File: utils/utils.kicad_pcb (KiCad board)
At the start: 2 copper layers, 26 parts, among them J1 1_AIN, J10 2_OUT, J11 EURORACK_CONN_16, J2 1_BIN, J3 1_GATE, J4 2_AIN, J5 2_BIN, J6 2_GATE, J7 1_~OUT, J8 2_~OUT, J9 1_OUT, Q1 2N7000, Q2 2N7000, U1 TL074

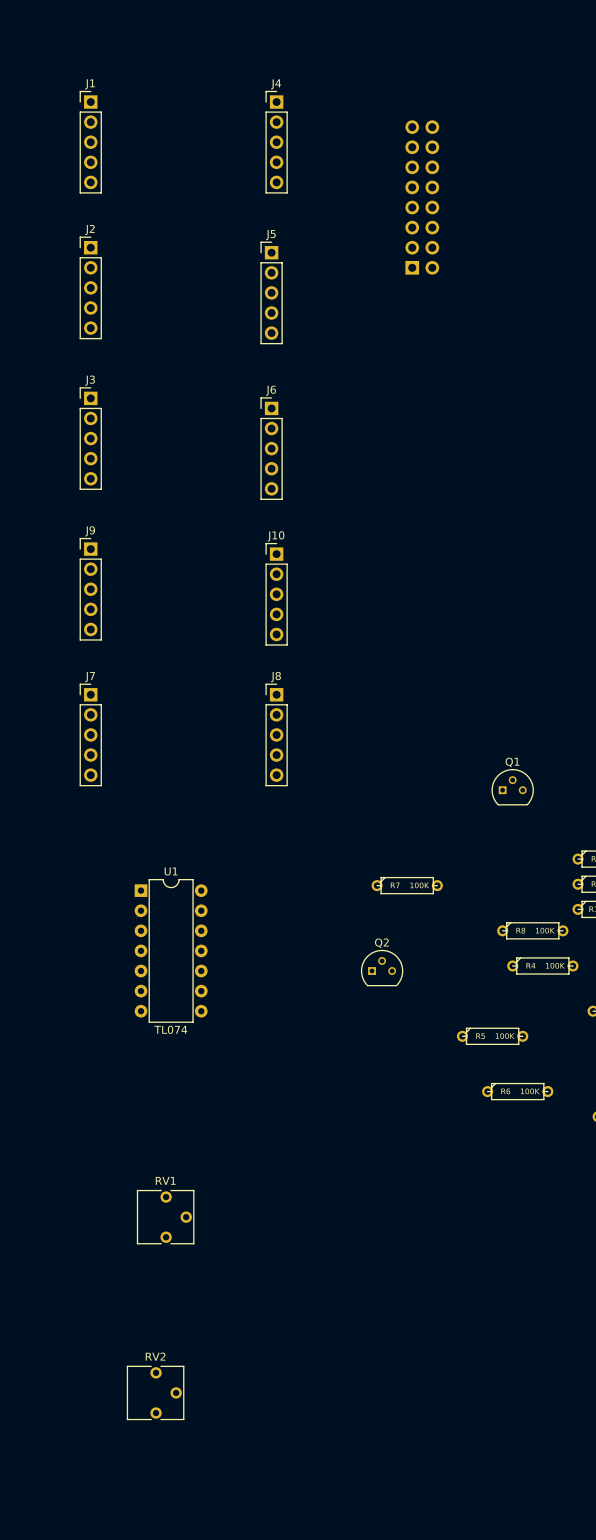
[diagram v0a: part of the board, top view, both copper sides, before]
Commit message: use jacks directly for horizontal
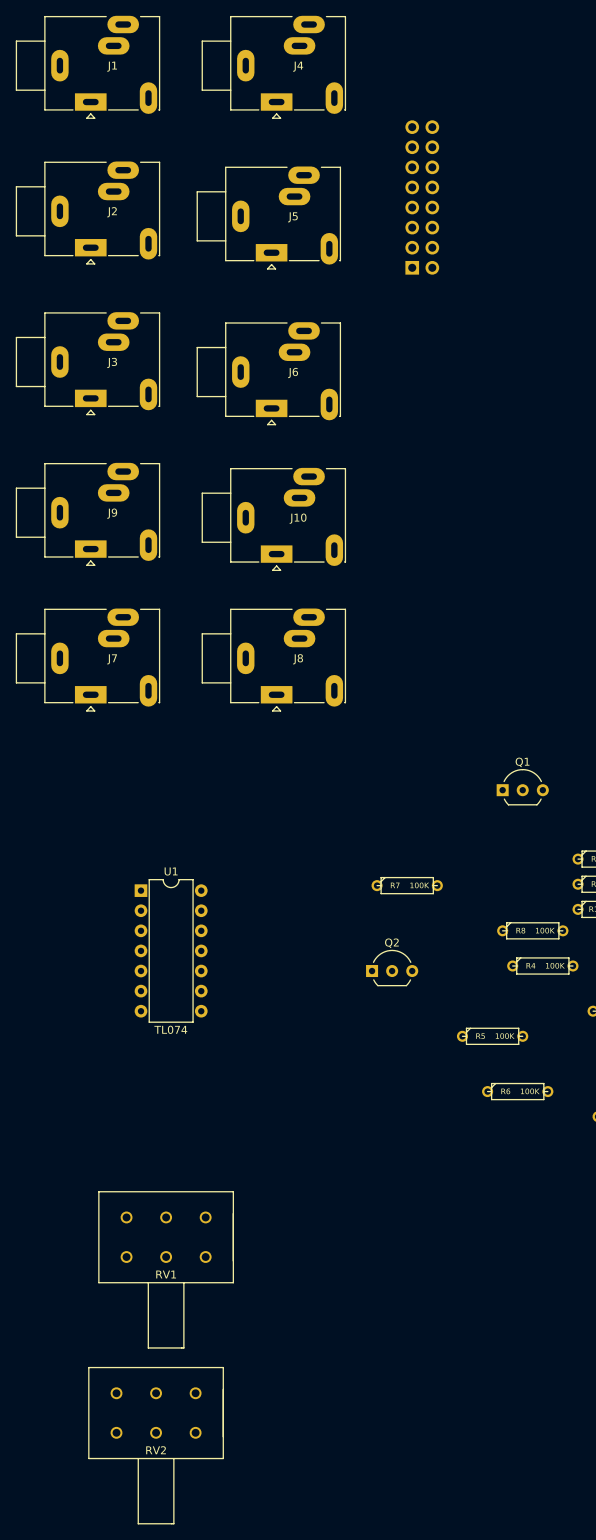
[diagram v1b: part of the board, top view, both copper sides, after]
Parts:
- J1, J10, J2, J3, J4, J5, J6, J7, J8, J9: footprint synth:3.5MM_Jack_Breakout_Vertical -> synth:Jack_3.5mm_Ledino_KB3SPRS_Horizontal
- Q1, Q2: footprint KiCad/TO_SOT_Packages_THT.pretty:TO-92_Molded_Narrow -> KiCad/TO_SOT_Packages_THT.pretty:TO-92_Inline_Wide
- RV1, RV2: footprint KiCad/Potentiometers.pretty:Potentiometer_Trimmer_Vishay_T73YP_Horizontal -> rdeterre/misc.pretty:Potentiometer_Bourns_PDB182-K_Dual

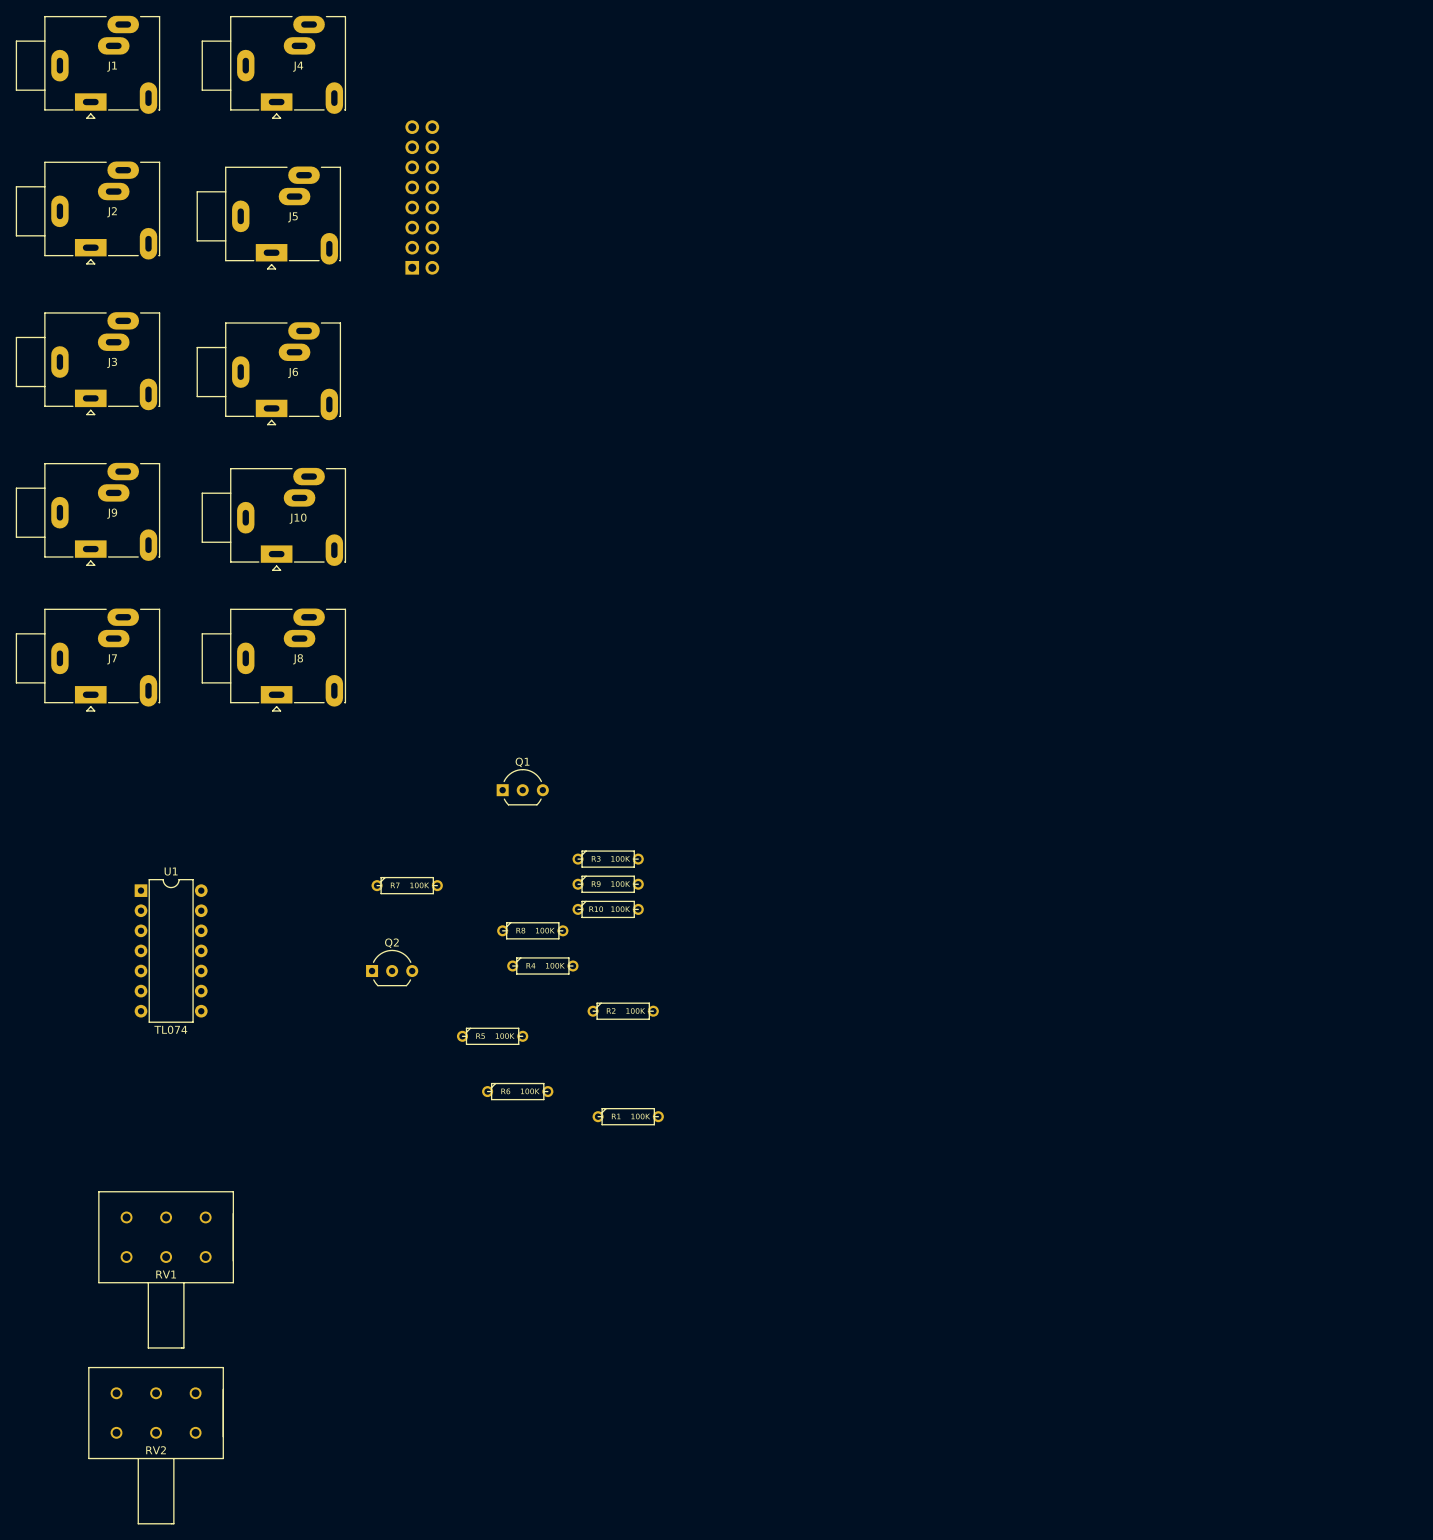
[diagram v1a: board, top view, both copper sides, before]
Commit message: switched fet with cd4066
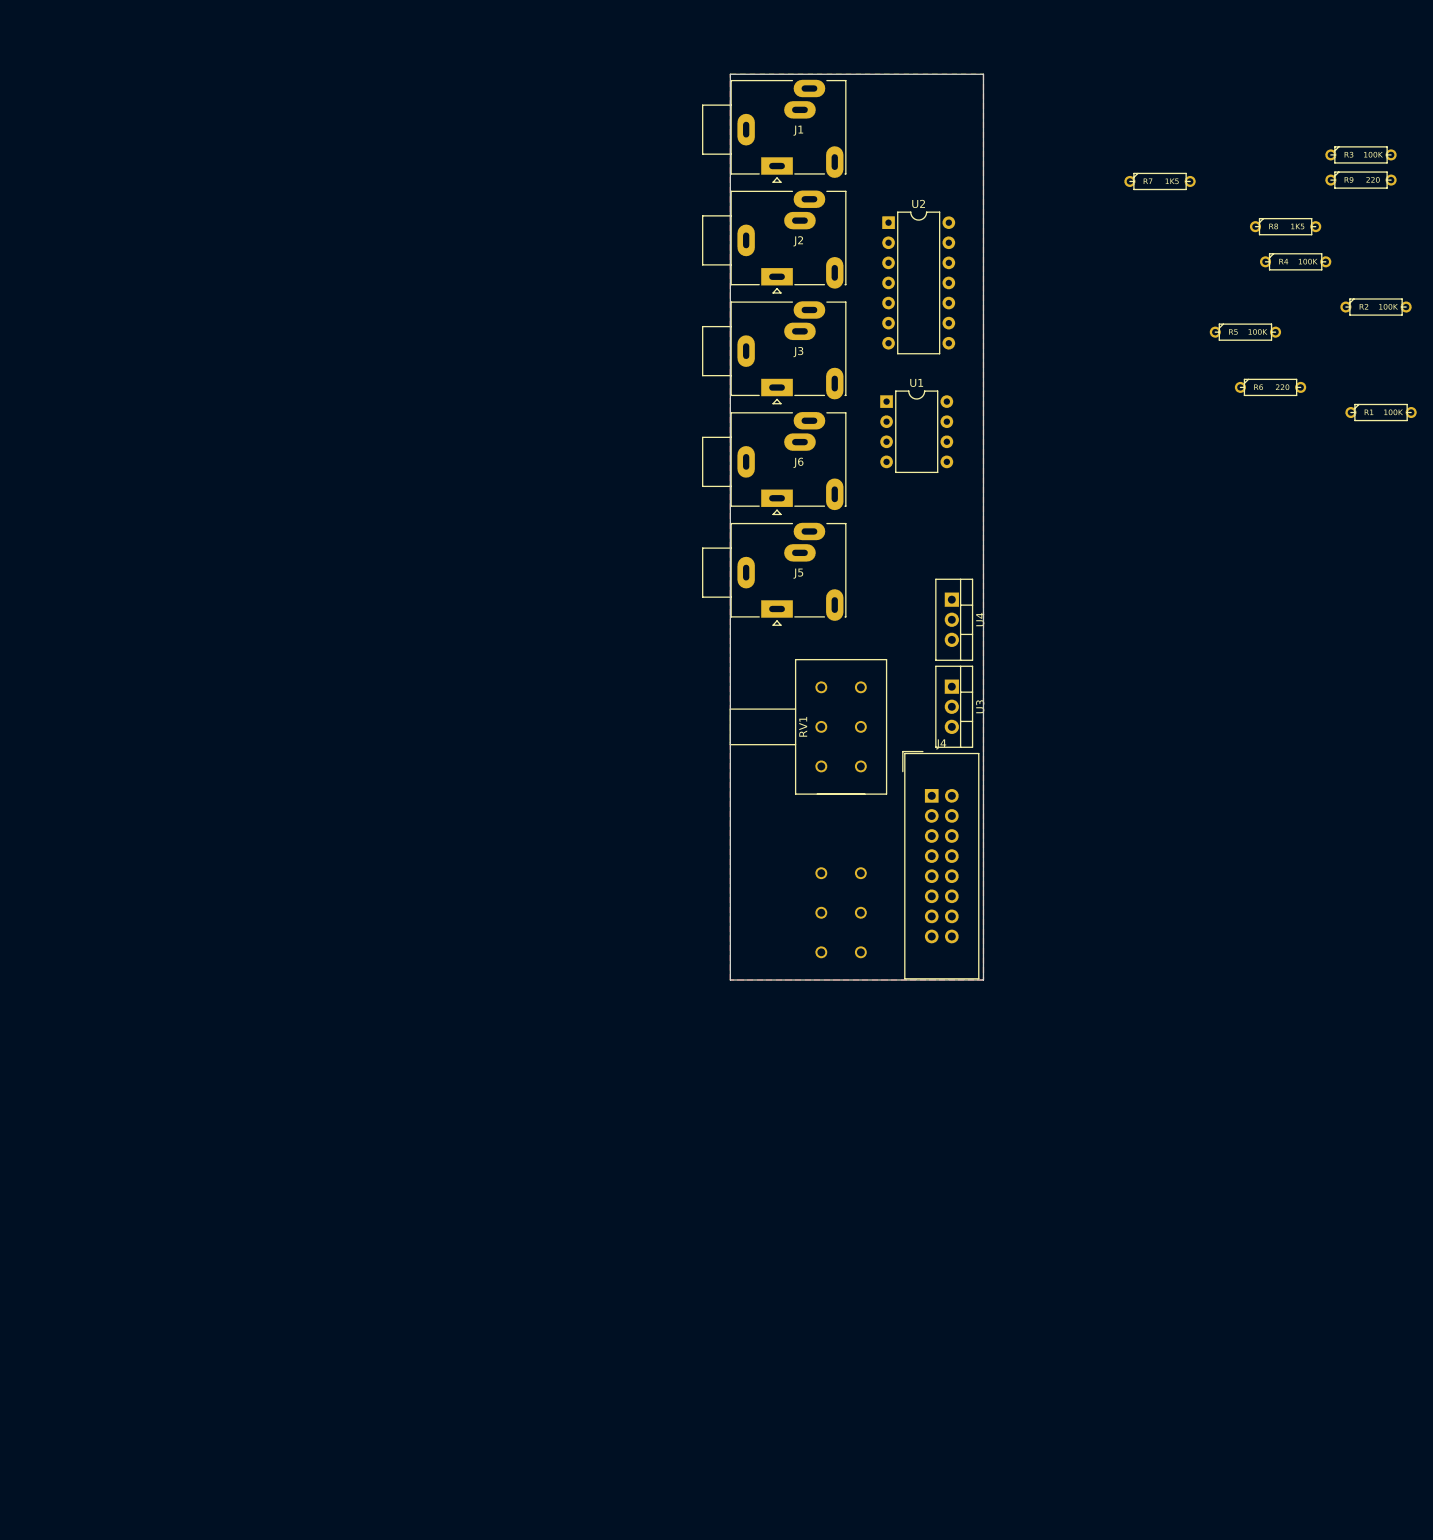
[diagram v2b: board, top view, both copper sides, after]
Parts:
- removed J10: 2_OUT, synth:Jack_3.5mm_Ledino_KB3SPRS_Horizontal
- removed J11: EURORACK_CONN_16, synth:EURORACK_16_IDC
- removed J7: 1_~OUT, synth:Jack_3.5mm_Ledino_KB3SPRS_Horizontal
- removed J8: 2_~OUT, synth:Jack_3.5mm_Ledino_KB3SPRS_Horizontal
- removed J9: 1_OUT, synth:Jack_3.5mm_Ledino_KB3SPRS_Horizontal
- removed Q1, Q2: 2N7000, KiCad/TO_SOT_Packages_THT.pretty:TO-92_Inline_Wide
- removed R10: 100K, 4ms/4ms-kicad-lib/4ms-footprints.pretty:Resistor_TH_300
- removed the RV1 at (26.7, 160.0)
- removed RV2: 200K, rdeterre/misc.pretty:Potentiometer_Bourns_PDB182-K_Dual
- added RV1: 100K, rdeterre/misc.pretty:Potentiometer_Bourns_PDB182-K_Dual, B.Cu at (112.0, 119.0)
- added RV1: 100K, rdeterre/misc.pretty:Potentiometer_Bourns_PDB182-K_Dual, F.Cu at (112.0, 95.5)
- added U2: 4066, KiCad/kicad-footprints/Package_DIP.pretty:DIP-14_W7.62mm, F.Cu at (118.0, 31.8)
- added U3: LM317L_TO92, KiCad/TO_SOT_Packages_THT.pretty:TO-220-3_Vertical, F.Cu at (126.0, 90.4)
- added U4: LM337L_TO92, KiCad/TO_SOT_Packages_THT.pretty:TO-220-3_Vertical, F.Cu at (126.0, 79.4)
- J1: value 1_AIN -> AIN
- J2: value 1_BIN -> BIN
- J3: value 1_GATE -> GATE
- J4: value 2_AIN -> EURORACK_CONN_16; footprint synth:Jack_3.5mm_Ledino_KB3SPRS_Horizontal -> synth:EURORACK_16_IDC
- J5: value 2_BIN -> ~OUT
- J6: value 2_GATE -> OUT
- R6, R9: value 100K -> 220
- R7, R8: value 100K -> 1K5
- U1: value TL074 -> TL072; footprint 4ms/4ms-kicad-lib/lib-footprints/4ms_Package_DIP.pretty:DIP-14_W7.62mm -> KiCad/kicad-footprints/Package_DIP.pretty:DIP-8_W7.62mm
- moved R5 130.3 mm to (163.1, 45.6)
- moved R1 130.3 mm to (180.3, 55.8)
- moved R2 130.3 mm to (179.6, 42.4)
- moved R3 130.3 mm to (177.7, 23.2)
- moved R4 130.3 mm to (169.5, 36.7)
- moved R9 130.3 mm to (177.7, 26.4)
- moved R6 130.3 mm to (166.3, 52.6)
- moved R7 130.3 mm to (152.3, 26.6)
- moved R8 130.3 mm to (168.2, 32.3)
- moved J4 120.6 mm to (123.5, 104.2)
- moved U1 112.7 mm to (117.8, 54.4)
- moved J1 87.1 mm to (103.9, 24.6)
- moved J2 86.8 mm to (103.9, 38.6)
- moved J3 86.8 mm to (103.9, 52.6)
- moved J5 78.2 mm to (103.9, 80.6)
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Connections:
- J1 pad T: 1_AIN -> AIN
- J2 pad T: 1_BIN -> BIN
- J3 pad T: 1_GATE -> GATE
- J5 pad T: 2_BIN -> ~OUT
- J5 pad TN: GND -> ~OUT
- J6 pad T: 2_GATE -> OUT
- J6 pad TN: +5V -> OUT
- R1 pad 1: 1_GATE -> Net-(R1-Pad1)
- R1 pad 2: GND -> AIN
- R2 pad 1: 2_GATE -> Net-(R1-Pad1)
- R2 pad 2: GND -> BIN
- R3 pad 1: Net-(Q1-Pad1) -> GATE
- R3 pad 2: 1_AIN -> GND
- R4 pad 1: Net-(Q2-Pad1) -> ~OUT
- R4 pad 2: 2_AIN -> Net-(R4-Pad2)
- R5 pad 1: Net-(Q1-Pad1) -> Net-(R4-Pad2)
- R5 pad 2: 1_BIN -> OUT
- R6 pad 1: Net-(Q2-Pad1) -> Net-(R6-Pad1)
- R6 pad 2: 2_BIN -> Net-(R6-Pad2)
- R7 pad 1: 1_~OUT -> Net-(R6-Pad2)
- R7 pad 2: Net-(R7-Pad2) -> GND
- R8 pad 1: 2_~OUT -> GND
- R8 pad 2: Net-(R10-Pad1) -> Net-(R8-Pad2)
- R9 pad 1: Net-(R7-Pad2) -> Net-(R8-Pad2)
- R9 pad 2: 1_OUT -> Net-(R9-Pad2)
- U1 pad 1: 1_~OUT -> Net-(RV1-Pad6)
- U1 pad 2: Net-(Q1-Pad1) -> Net-(R1-Pad1)
- U1 pad 4: +12V -> -12V
- U1 pad 6: Net-(R7-Pad2) -> Net-(R4-Pad2)
- U1 pad 7: 1_OUT -> OUT
- U1 pad 8: 2_~OUT -> +12V
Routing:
- added copper zone on F.Cu, net GND
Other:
- board outline added: 32 x 114.5 mm

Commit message: pcb mostly laid out
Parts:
- removed the RV1 at (112.0, 119.0)
- added J7: Conn_01x04, imciner2/KiCad-Libraries/modules/Connectors.pretty:CONN_2.54mm_1x04, F.Cu at (115.0, 49.4)
- added J8: Conn_01x05, imciner2/KiCad-Libraries/modules/Connectors.pretty:CONN_2.54mm_1x05, F.Cu at (128.0, 50.7)
- U3: value LM317L_TO92 -> LM317
- U4: value LM337L_TO92 -> LM337
- moved R1 67.5 mm to (118.2, 29.2), turned to 180 degrees
- moved R2 62.4 mm to (118.2, 31.8), turned to 180 degrees
- moved U3 62.0 mm to (126.0, 28.4)
- moved U4 61.7 mm to (126.0, 17.7)
- moved R3 60.6 mm to (118.2, 34.5), turned to 180 degrees
- moved R9 60.3 mm to (118.2, 16.8)
- moved R4 59.7 mm to (115.5, 62.2), turned to 270 degrees
- moved R6 54.7 mm to (118.2, 26.5), turned to 180 degrees
- moved R5 54.7 mm to (115.5, 72.4), turned to 270 degrees
- moved R8 51.5 mm to (118.2, 20.0), turned to 180 degrees
- moved R7 34.3 mm to (118.2, 23.2)
- moved U1 18.8 mm to (126.5, 71.0), turned to 180 degrees
- moved U2 8.76 mm to (117.6, 40.5)
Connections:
- U2 pad 10: (no net) -> 4066_10
- U2 pad 11: (no net) -> 4066_11
- U2 pad 12: (no net) -> 4066_12
- U2 pad 3: (no net) -> 4066_3
- U2 pad 4: (no net) -> 4066_4
- U2 pad 5: (no net) -> 4066_5
- U2 pad 6: (no net) -> 4066_6
- U2 pad 8: (no net) -> 4066_8
- U2 pad 9: (no net) -> 4066_9
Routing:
- net -12V: track 0.00 -> 89.8 mm
- net +12V: track 0.00 -> 88.3 mm
- net Net-(R1-Pad1): track 0.00 -> 78.2 mm, vias 0 -> 1
- net +5V: track 0.00 -> 72.4 mm, vias 0 -> 2
- net Net-(RV1-Pad6): track 0.00 -> 69.9 mm, vias 0 -> 1
- net ~OUT: track 0.00 -> 51.1 mm
- net Net-(R9-Pad2): track 0.00 -> 47.8 mm
- net GATE: track 0.00 -> 37.3 mm
- net OUT: track 0.00 -> 26.1 mm
- net Net-(R6-Pad1): track 0.00 -> 18.4 mm
- net Net-(R6-Pad2): track 0.00 -> 15.7 mm
- net Net-(R8-Pad2): track 0.00 -> 15.1 mm
- net BIN: track 0.00 -> 13.3 mm
- net AIN: track 0.00 -> 13.2 mm
- net Net-(RV1-Pad3): track 0.00 -> 12.1 mm
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- added copper zone on B.Cu, net GND
- removed copper zone on F.Cu, net GND
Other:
- board size 32 x 114.5 mm -> 50.2 x 114.5 mm
- board text added: "TODO: how long is shaft?"
- board text added: "TODO: what’s the orientation of this?"

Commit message: cleanup
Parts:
- added RV1: 100K, rdeterre/misc.pretty:Potentiometer_Bourns_PDB182-K_Dual, B.Cu at (107.2, 115.5)
- moved RV1 4.85 mm to (107.2, 96.5)
- moved R9 2.50 mm to (118.2, 19.2)
- moved R8 1.75 mm to (118.2, 21.8)
- moved R7 1.00 mm to (118.2, 24.2)
- moved R3 0.25 mm to (118.2, 34.2)
- moved R6 0.25 mm to (118.2, 26.8)
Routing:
- net Net-(R1-Pad1): track 78.2 -> 47.0 mm
- net Net-(RV1-Pad6): track 69.9 -> 52.9 mm
- net Net-(RV1-Pad3): track 12.1 -> 0.00 mm
- net Net-(R9-Pad2): track 47.8 -> 43.8 mm
- net Net-(R6-Pad2): track 15.7 -> 16.5 mm
- net GATE: track 37.3 -> 37.8 mm
- added copper zone on F.Cu, net GND
- removed copper zone on B.Cu, net GND
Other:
- board size 50.2 x 114.5 mm -> 32.2 x 114.5 mm
- board text added: "TODO: what is standard spacing for knobs?"
- board text removed: "TODO: how long is shaft?"
